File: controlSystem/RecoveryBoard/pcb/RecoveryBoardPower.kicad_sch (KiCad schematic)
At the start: 65 parts, among them J1 Conn_01x06, J10 Conn_01x02, J2 Thermistor, J3 Conn_01x04, J8 Conn_01x06, Q1 SI7465DP-T1-E3, U2 MP26123DR-LF-Z, U3 TPS63070

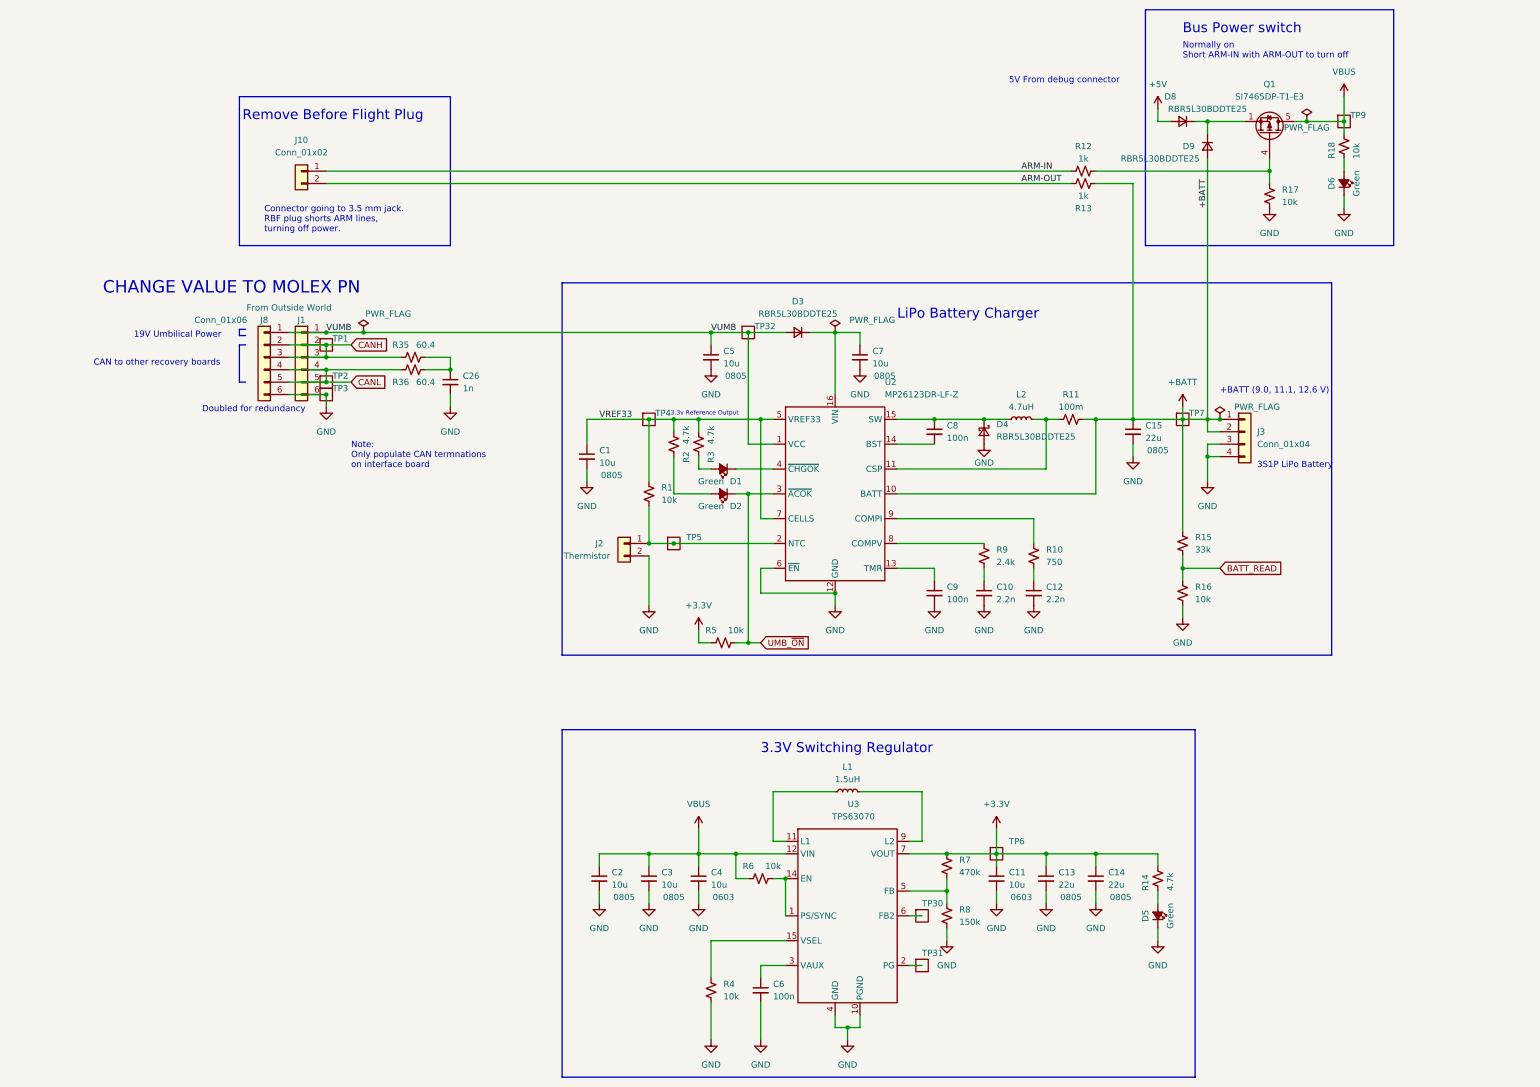
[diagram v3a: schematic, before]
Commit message: v3.1. Cap to deal with spikes on RBF, 100k on main Q pull down, better notes on schematic for part numbers, moved Vbatt pickoff to after main Q.
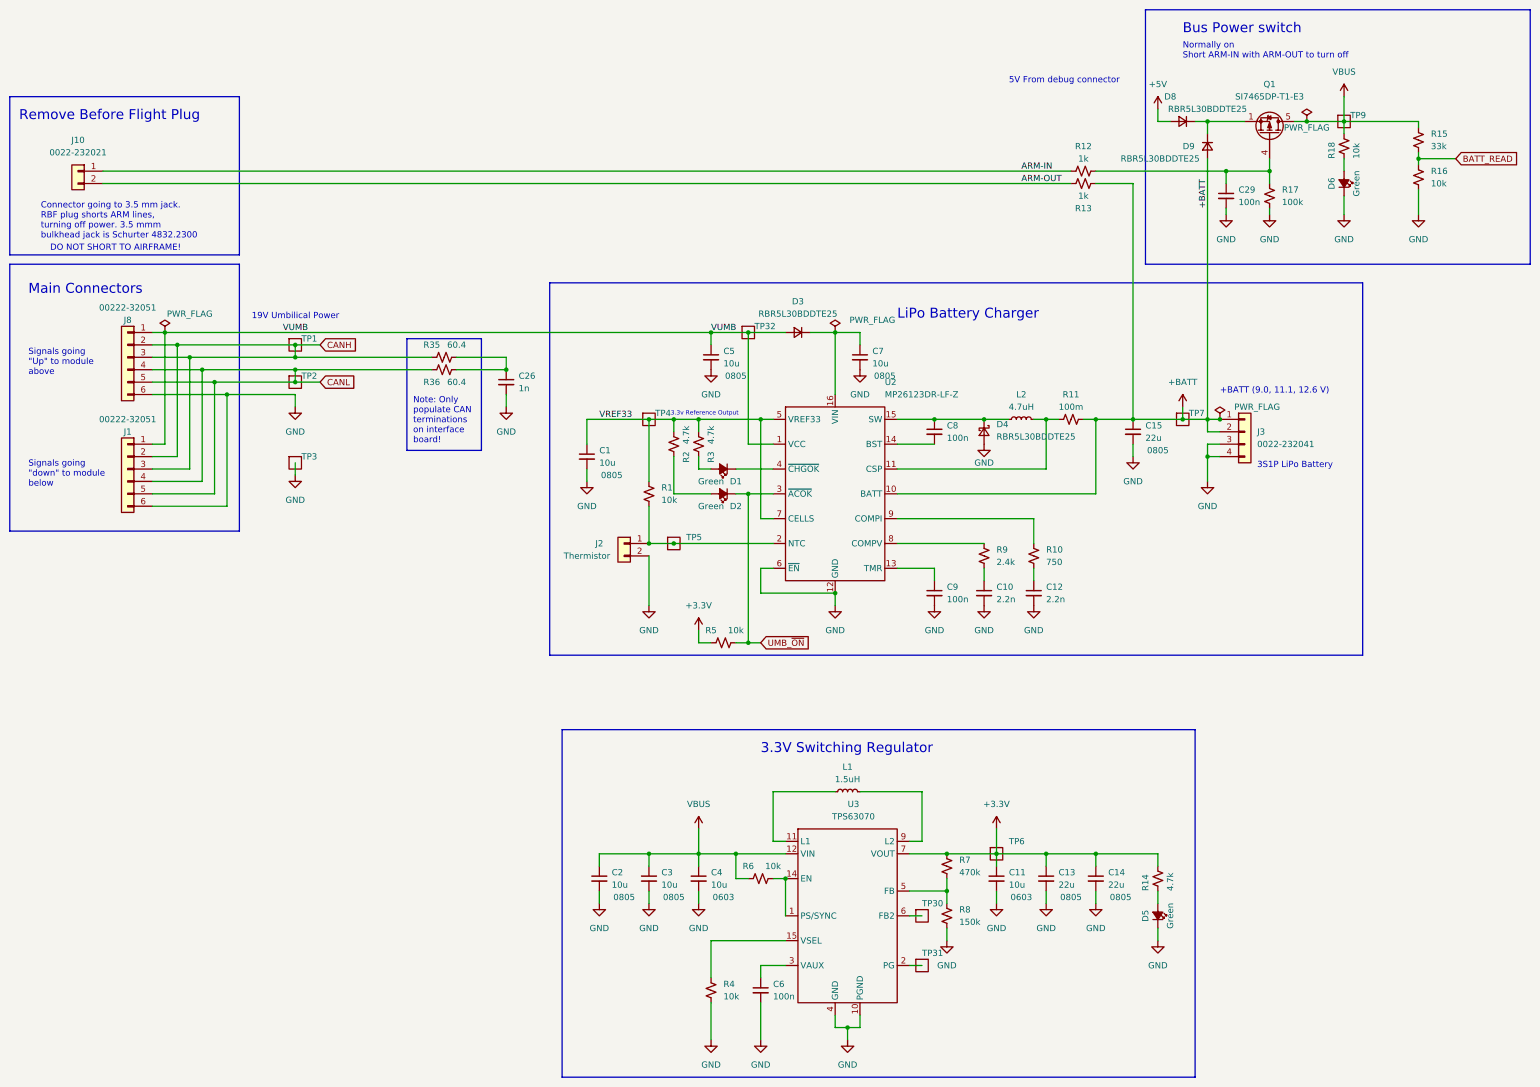
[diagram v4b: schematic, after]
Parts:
- added C29: 100n, Capacitor_SMD:C_0603_1608Metric, symbol Device:C_Small
- J1, J8: value Conn_01x06 -> 00222-32051
- J10: value Conn_01x02 -> 0022-232021
- J3: value Conn_01x04 -> 0022-232041
- R17: value 10k -> 100k
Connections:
- net +BATT: no longer R15.1
- net GND: now also C29.2
- net VBUS: now also R15.1
- net at Q1.4 (G), R12.2, R17.1: now also C29.1
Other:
- note added: "Connector going to 3.5 mm jack. RBF plug shorts ARM lines, turning off power. 3.5 mmm bulkhead jack is Schurter 4832.2300"
- note added: "DO NOT SHORT TO AIRFRAME!"
- note added: "Main Connectors"
- note added: "Note: Only populate CAN terminations on interface board!"
- note added: "Signals going "Up" to module above"
- note added: "Signals going "down" to module below"
- note removed: "CAN to other recovery boards"
- note removed: "CHANGE VALUE TO MOLEX PN"
- note removed: "Connector going to 3.5 mm jack. RBF plug shorts ARM lines, turning off power."
- note removed: "Doubled for redundancy"
- note removed: "Note: Only populate CAN termnations on interface board"
- title: (none) -> Electromechanical Recovery System Board
- moved on the sheet: C26, J1, J10, J8, R15, R16, R35, R36, TP1, TP2

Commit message: Stuffing four more v3.0 PCBs and discovered everything wasn't updated. Fixed BOM, fixed a lot of schematic errors especially in symbols, fixed some footprint errors, synchronized schematic and pcb, and general cleanup. This board is still v3.1.
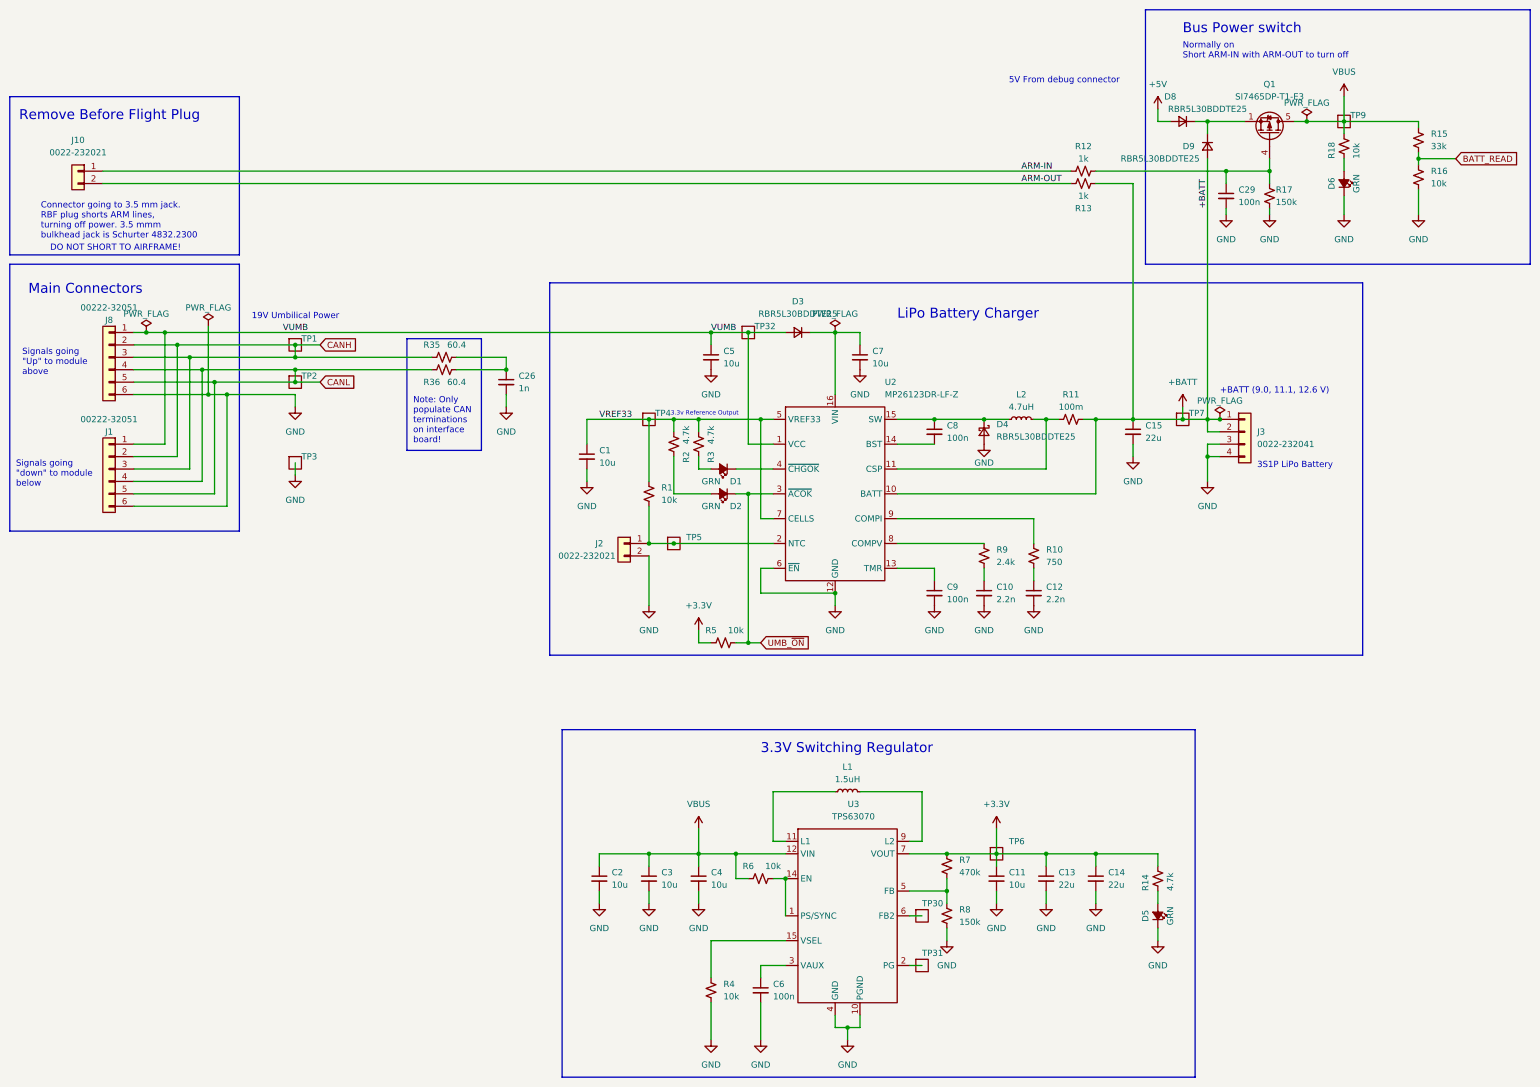
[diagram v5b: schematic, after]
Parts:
- C1, C2, C3, C5, C7: DPN (none) -> 490-18663-1-ND; DST (none) -> DigiKey; Field4 0805 -> (none); MFR (none) -> Murata; MPN (none) -> GRM21BR61H106KE43L
- C10, C12: DPN (none) -> 1276-6530-1-ND; DST (none) -> DigiKey; MFR (none) -> Samsung Microelectronics; MPN (none) -> CL10B222KB8WPNC
- C11, C4: DPN (none) -> 490-12323-1-ND; DST (none) -> DigiKey; Field4 0603 -> (none); MFR (none) -> Murata; MPN (none) -> GRT188R61E106ME13D
- C13, C14, C15: DPN (none) -> 490-12389-1-ND; DST (none) -> DigiKey; Field4 0805 -> (none); MFR (none) -> Murata
- C26: DPN (none) -> 1276-6991-1-ND; DST (none) -> DigiKey; MFR (none) -> Samsung Microelectronics; MPN (none) -> CL10B102KB85PNL
- C29, C6, C8, C9: DPN (none) -> 1276-6854-1-ND; DST (none) -> DigiKey; MFR (none) -> Samsung Microelectronics; MPN (none) -> CL10B104KB8WPNC
- D1, D2, D5, D6: value Green -> GRN; DPN (none) -> 732-4971-1-ND; DST (none) -> DigiKey; MFR (none) -> Wurth; MPN (none) -> 150060GS75000
- D3, D4, D8, D9: DPN (none) -> 846-RBR5L30BDDTE25CT-ND; DST (none) -> DigiKey; MFR (none) -> Rohm; MPN (none) -> RBR5L30BDDTE25
- J1, J8: DPN (none) -> WM4204-ND; DST (none) -> DigiKey; Field4 From Outside World -> (none); MFR (none) -> Molex; MPN (none) -> 22232061
- J10: DPN (none) -> 900-0022232021-ND; DST (none) -> DigiKey; MFR (none) -> Molex; MPN (none) -> 22232021
- J2: value Thermistor -> 0022-232021; DPN (none) -> 900-0022232021-ND; DST (none) -> DigiKey; MFR (none) -> Molex; MPN (none) -> 22232021
- J3: DPN (none) -> WM4202-ND; DST (none) -> DigiKey; MFR (none) -> Molex; MPN (none) -> 22232041
- L1: DPN (none) -> 541-1235-1-ND; DST (none) -> DigiKey; MFR (none) -> Vishay
- L2: DPN (none) -> 541-1222-1-ND; DST (none) -> DigiKey; MFR (none) -> Vishay
- Q1: DPN (none) -> SI7141DP-T1-GE3CT-ND; DST (none) -> DigiKey; MFR (none) -> Vishay; MPN (none) -> SI7141DP-T1-GE3
- R1, R16, R18, R4, R5, R6: DPN (none) -> 311-10.0KHRCT-ND; DST (none) -> DigiKey; MFR (none) -> Yageo; MPN (none) -> RC0603FR-0710KL
- R10: DPN (none) -> 311-750HRCT-ND; DST (none) -> DigiKey; MFR (none) -> Yageo; MPN (none) -> RC0603FR-07750RL
- R11: DPN (none) -> CSR1206FTR100CT-ND; DST (none) -> DigiKey; MFR (none) -> Stackpole; MPN (none) -> CSR1206FTR100
- R12, R13: DPN (none) -> 311-1.00KHRCT-ND; DST (none) -> DigiKey; MFR (none) -> Yageo; MPN (none) -> RC0603FR-071KL
- R14, R2, R3: DPN (none) -> 311-4.70KHRCT-ND; DST (none) -> DigiKey; MFR (none) -> Yageo; MPN (none) -> RC0603FR-074K7L
- R15: DPN (none) -> 311-33.0KHRCT-ND; DST (none) -> DigiKey; MFR (none) -> Yageo; MPN (none) -> RC0603FR-0733KL
- R17: value 100k -> 150k; DPN (none) -> 311-150KHRCT-ND; DST (none) -> DigiKey; MFR (none) -> Yageo; MPN (none) -> RC0603FR-07150KL
- R35, R36: DPN (none) -> 311-60.4HRCT-ND; DST (none) -> DigiKey; MFR (none) -> Yageo; MPN (none) -> RC0603FR-0760R4L
- R7: DPN (none) -> 311-470KHRCT-ND; DST (none) -> DigiKey; MFR (none) -> Yageo; MPN (none) -> RC0603FR-07470KL
- R8: DPN (none) -> 311-150KHRCT-ND; DST (none) -> DigiKey; MFR (none) -> Yageo; MPN (none) -> RC0603FR-07150KL
- R9: DPN (none) -> 311-2.40KHRCT-ND; DST (none) -> DigiKey; MFR (none) -> Yageo; MPN (none) -> RC0603FR-072K4L
- TP1, TP2, TP3, TP32, TP4, TP5, TP7, TP9: now left out of the parts list
- U2: DPN (none) -> 1589-1609-1-ND; DST (none) -> DigiKey; MFR (none) -> Monolithic Power Systems; MPN (none) -> MP26123DR-LF-Z
- U3: DPN (none) -> 296-44874-1-ND; DST (none) -> DigiKey; MFR (none) -> Texas Instruments; MPN (none) -> TPS63070RNMR
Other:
- moved on the sheet: J1, J8
